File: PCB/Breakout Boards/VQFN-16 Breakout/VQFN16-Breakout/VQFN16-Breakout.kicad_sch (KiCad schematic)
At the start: 3 parts, among them J1 Conn_01x08_Pin, J2 Conn_01x08_Pin

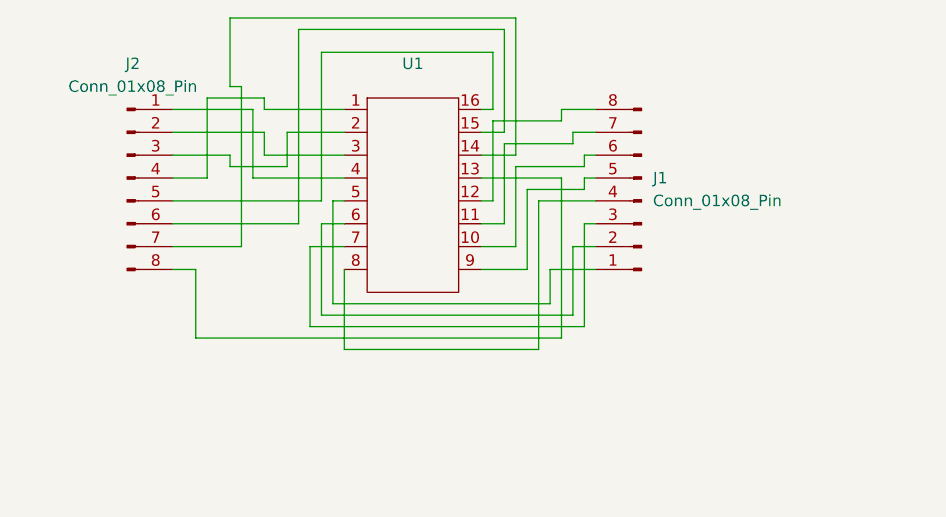
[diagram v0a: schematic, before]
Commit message: VQFN16
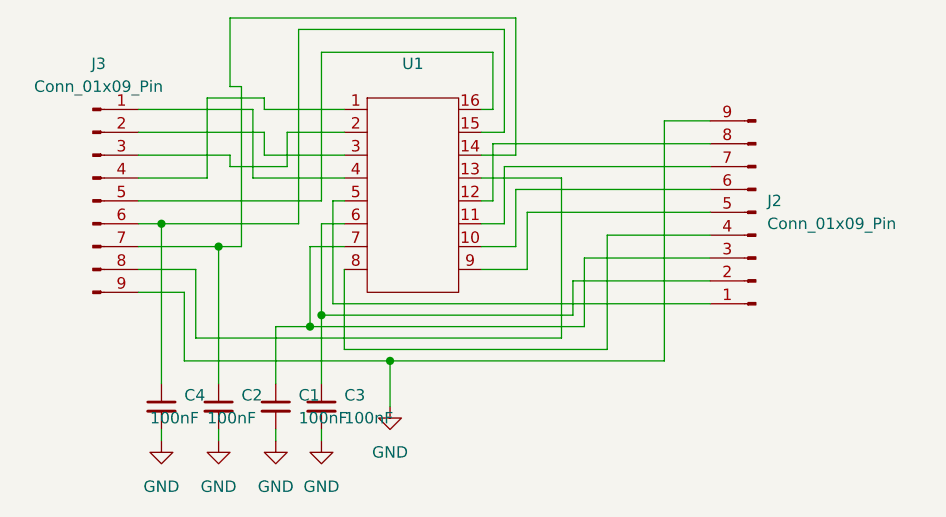
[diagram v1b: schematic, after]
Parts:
- removed J1, J2: Conn_01x08_Pin, Connector_PinHeader_2.54mm:PinHeader_1x08_P2.54mm_Vertical, symbol Connector:Conn_01x08_Pin
- added C1, C2, C3, C4: 100nF, Capacitor_SMD:C_0805_2012Metric, symbol Device:C_Small
- added J2, J3: Conn_01x09_Pin, Connector_PinHeader_2.54mm:PinHeader_1x09_P2.54mm_Vertical, symbol Connector:Conn_01x09_Pin
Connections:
- net at U1.4: now also J3.1 (Pin_1)
- net at U1.3: now also J3.2 (Pin_2)
- net at U1.2: now also J3.3 (Pin_3)
- net at U1.1: now also J3.4 (Pin_4)
- net at U1.16: now also J3.5 (Pin_5)
- net at U1.15: now also C4.1, J3.6 (Pin_6)
- net at U1.14: now also C2.1, J3.7 (Pin_7)
- net at U1.13: now also J3.8 (Pin_8)
- net at U1.10: now also J2.6 (Pin_6)
- net at U1.11: now also J2.7 (Pin_7)
- net at U1.12: now also J2.8 (Pin_8)
- net at U1.5: now also J2.1 (Pin_1)
- net at U1.6: now also C3.1, J2.2 (Pin_2)
- net at U1.7: now also C1.1, J2.3 (Pin_3)
- net at U1.8: now also J2.4 (Pin_4)
- net at U1.9: now also J2.5 (Pin_5)
- new net GND: C1.2, C2.2, C3.2, C4.2, J2.9 (Pin_9), J3.9 (Pin_9)
